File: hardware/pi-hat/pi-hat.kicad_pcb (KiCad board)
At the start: 2 copper layers, 65 x 56 mm, 88 parts, among them J1 PWR IN, J10 6-8, J11 PWM0, J12 PWM1, J13 KLPX-0848A-2-B, J14 KLPX-0848A-2-R, J2 A-F, J3 40HAT, J4 G-M, J5 N-Q, J6 PANEL_PWR, J7 PANEL_CTL, J8 2-5, J9 WP, Q1 DMG2305UX, Q2 DMMT5401, Q3 DMN6075S, Q4 ?, Q5 DMN6075S, U1 CAT24C32, U10 L78L33_SOT89, U11 L78L33_SOT89, U12 PCM5122PW, U2 CM1293A, U3 CM1293A, U4 CM1293A, U5 CM1293A, U6 CM1293A, U7 CM1293A, U8 MCP23S17_SO, U9 MCP23S17_SO

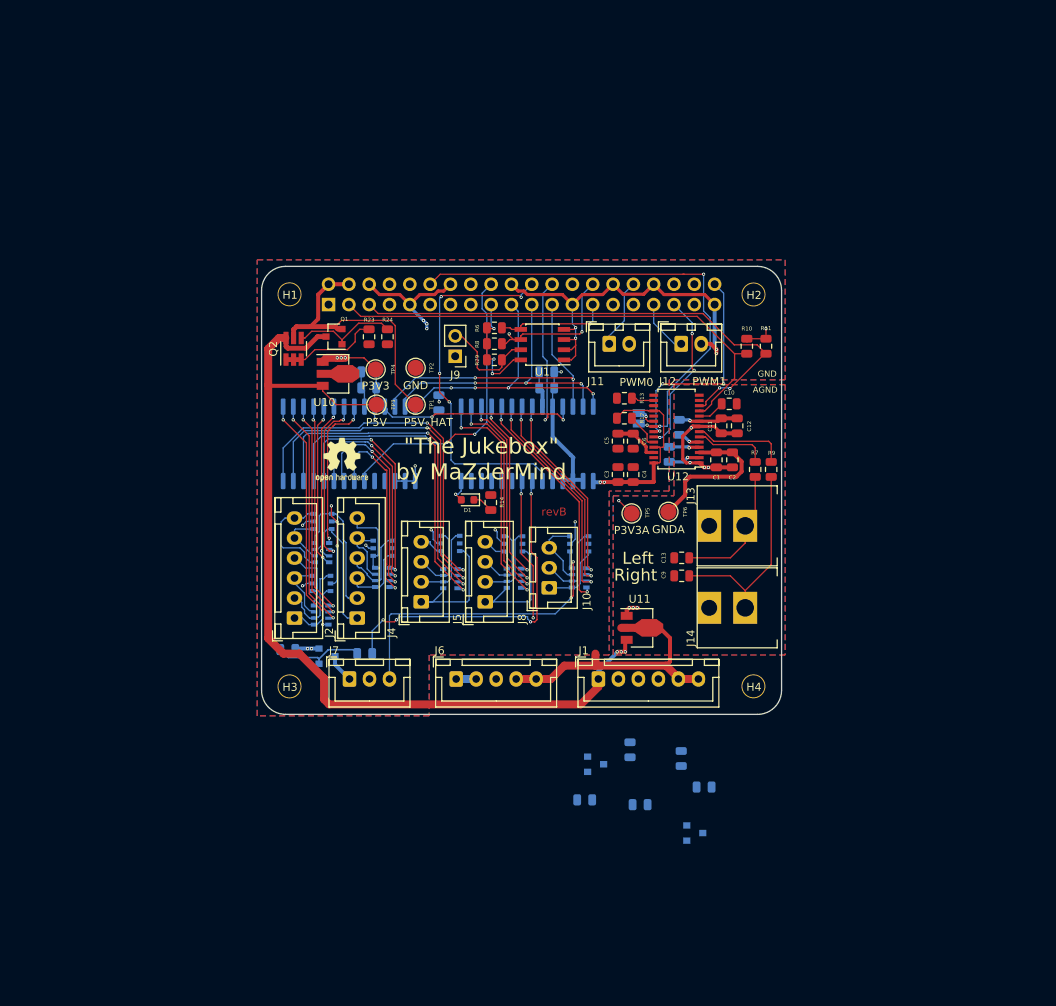
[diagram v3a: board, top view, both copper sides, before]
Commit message: re-configure board. route 30V and GND
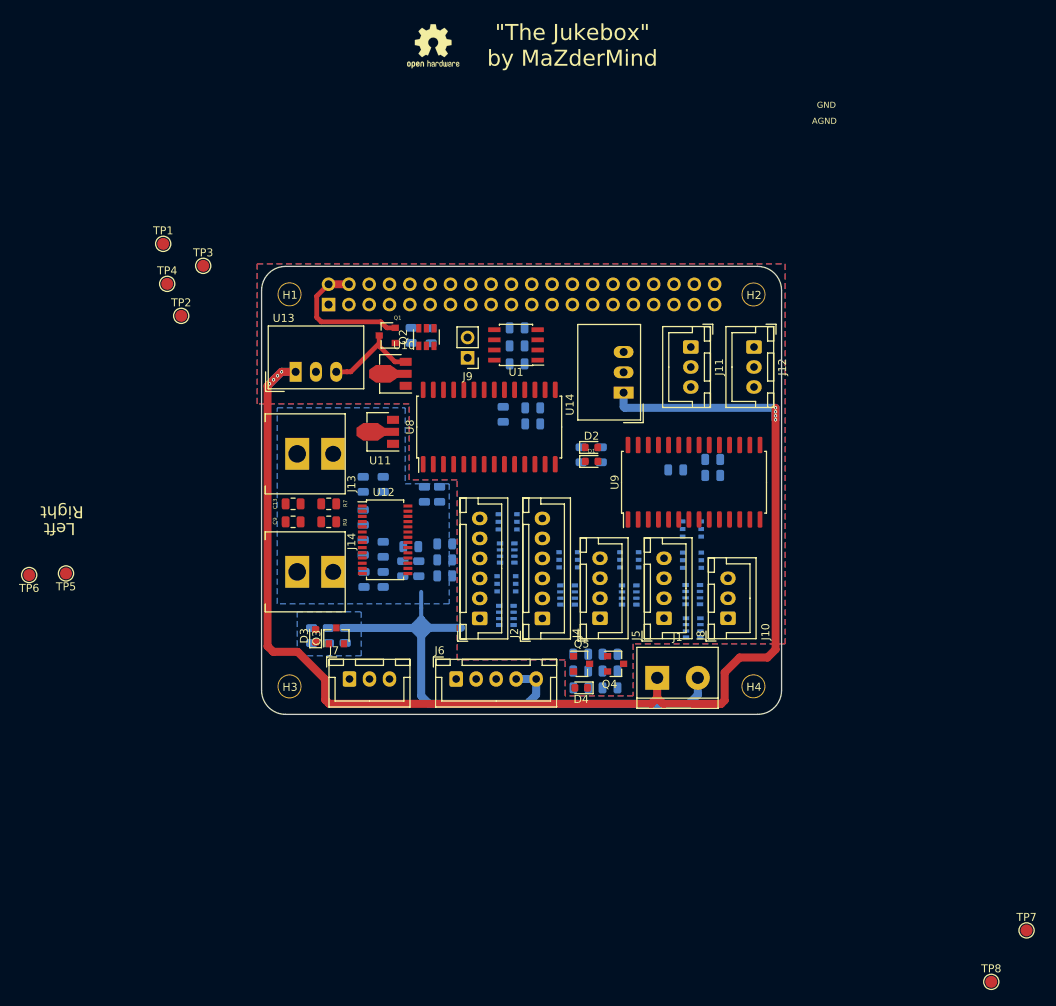
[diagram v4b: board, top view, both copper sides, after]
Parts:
- removed JP2: Jumper_NO_Small, Jumper:SolderJumper-2_P1.3mm_Open_Pad1.0x1.5mm
- added D3: SOLENOID, LED_SMD:LED_0603_1608Metric, F.Cu at (85.3, 107.0)
- added D4: PANEL, LED_SMD:LED_0603_1608Metric, F.Cu at (118.5, 113.5)
- added D5: MMSZ5239B-7-F (9.1V), Diode_SMD:D_0805_2012Metric, B.Cu at (122.1, 109.3)
- added R17: 10k, Resistor_SMD:R_0805_2012Metric, B.Cu at (130.3, 86.2)
- added R18: 100R, Resistor_SMD:R_0805_2012Metric, B.Cu at (84.8, 107.0)
- added R19: 100R, Resistor_SMD:R_0805_2012Metric, B.Cu at (122.1, 113.5)
- added R20: 100R, Resistor_SMD:R_0805_2012Metric, B.Cu at (121.0, 84.4)
- added TP7: P30V, TestPoint:TestPoint_Pad_D1.5mm, F.Cu at (174.2, 143.8)
- added TP8: P5V_LED, TestPoint:TestPoint_Pad_D1.5mm, F.Cu at (169.8, 150.2)
- added U13: TSR_2-2450, Converter_DCDC:Converter_DCDC_TRACO_TSR-1_THT, F.Cu at (82.8, 74.0)
- added U14: TSR_2-2450, Converter_DCDC:Converter_DCDC_TRACO_TSR-1_THT, F.Cu at (123.8, 76.6)
- C1, C10, C11, C12, C2, C3, C4, C5, C6, JP1, R10, R11, R12, R13, R14, R23, R24, R29, R6, R8: moved to B.Cu
- D1: value LED GN -> READY
- D2: value ? -> PLAY; footprint Diode_SMD:D_0805_2012Metric -> LED_SMD:LED_0603_1608Metric; moved to F.Cu
- J1: value PWR IN -> PWR_IN; footprint Connector_JST:JST_XH_B6B-XH-A_1x06_P2.50mm_Vertical -> TerminalBlock:TerminalBlock_bornier-2_P5.08mm
- J11: value PWM0 -> LED0; footprint Connector_JST:JST_XH_B2B-XH-A_1x02_P2.50mm_Vertical -> Connector_JST:JST_XH_B3B-XH-A_1x03_P2.50mm_Vertical
- J12: value PWM1 -> LED1; footprint Connector_JST:JST_XH_B2B-XH-A_1x02_P2.50mm_Vertical -> Connector_JST:JST_XH_B3B-XH-A_1x03_P2.50mm_Vertical
- Q2: footprint Package_TO_SOT_SMD:SOT-23-6_Handsoldering -> Package_TO_SOT_SMD:SOT-23-6
- Q3, Q5, U8, U9: moved to F.Cu
- Q4: value ? -> DMP4065S; moved to F.Cu
- R16: value 10k -> 5.6k
- R4: value 10k -> NC
- TP1, TP2, TP3, TP4, TP5, TP6: footprint TestPoint:TestPoint_Pad_D2.0mm -> TestPoint:TestPoint_Pad_D1.5mm
- moved TP6 80.3 mm to (49.5, 99.4), turned to 180 degrees
- moved TP5 71.1 mm to (54.1, 99.2), turned to 180 degrees
- moved J13 64.6 mm to (79.0, 84.2), turned to 0 degrees
- moved J14 64.2 mm to (79.0, 99.0), turned to 0 degrees
- moved R11 58.1 mm to (91.3, 100.0)
- moved R9 55.7 mm to (86.9, 92.8), turned to 0 degrees
- moved R10 54.0 mm to (93.8, 100.0)
- moved R7 53.5 mm to (86.9, 90.5), turned to 0 degrees
- moved OSHW1 52.9 mm to (100.0, 33.3)
- moved C13 49.0 mm to (82.5, 90.5)
- moved C9 49.0 mm to (82.5, 92.8)
- moved C2 46.3 mm to (91.2, 88.1)
- moved C12 45.5 mm to (96.2, 98.6)
- moved D2 45.1 mm to (119.8, 83.5)
- moved C10 43.6 mm to (97.2, 95.8), turned to 180 degrees
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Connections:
- net /IO_INT_A renamed /INT_U8
- net /IO_INT_B renamed /INT_U9
- net /LED renamed /READY_LED
- net /PANEL_30V renamed /PANEL_30V_OUT
- net /PANEL_SW renamed /PANEL_CTRL
- net /SOLENOID renamed /PANEL_SOLENOID_OUT
- net /SOLENOID_SW renamed /SOLENOID_CTRL
- D2 pad 1: /P30V -> Net-(D2-Pad1)
- D2 pad 2: Net-(D2-Pad2) -> /PLAY_LED
- J1 pad 1: /P5V -> /P30V
- J1 pad 2: (no net) -> GND
- J11 pad 1: /PWM0 -> /P5V_LED
- J11 pad 2: GND -> /PWM0
- J12 pad 1: /PWM1 -> /P5V_LED
- J12 pad 2: GND -> /PWM1
- J3 pad 19: /SPI_MISO -> /SPI_MOSI
- J3 pad 21: /SPI_MOSI -> /SPI_MISO
- J3 pad 24: /SPI_CS -> /SPI_CS_U8
- J3 pad 26: (no net) -> /SPI_CS_U9
- Q4 pad 1: Net-(D2-Pad2) -> Net-(D5-Pad2)
- R16 pad 2: Net-(D2-Pad2) -> Net-(D5-Pad2)
- R4 pad 1: Net-(D2-Pad2) -> Net-(D5-Pad2)
- R5 pad 2: /SPI_CS -> /SPI_CS_U8
- RN2 pad 7: /F -> /E
- RN2 pad 8: /E -> /F
- U12 pad 20: /DAC_SYSCLK -> (no net)
- U8 pad 11: /SPI_CS -> /SPI_CS_U8
- U8 pad 18: GND -> /P3V3
- U9 pad 11: /SPI_CS -> /SPI_CS_U9
- U9 pad 15: /P3V3 -> GND
- U9 pad 18: GND -> /P3V3
- U9 pad 27: (no net) -> /PLAY_LED
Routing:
- net /P30V: track 0.00 -> 169.5 mm, vias 0 -> 8
- net /P5V: track 116.6 -> 12.3 mm, vias 3 -> 0
- net GND: track 141.1 -> 71.2 mm, vias 19 -> 0
- net /I2C_SCL: track 63.5 -> 0.00 mm, vias 2 -> 0
- net /I2C_SDA: track 61.8 -> 0.00 mm
- net /PCM_CLK: track 60.2 -> 0.00 mm, vias 3 -> 0
- net /P3V3: track 59.1 -> 0.00 mm, vias 9 -> 0
- net /INT_U9: track 46.5 -> 0.00 mm, vias 4 -> 0
- net /SPI_CS: track 45.0 -> 0.00 mm, vias 3 -> 0
- net /Q: track 44.7 -> 0.00 mm, vias 2 -> 0
- net /P: track 43.9 -> 0.00 mm, vias 2 -> 0
- net /O: track 42.7 -> 0.00 mm, vias 2 -> 0
- net /SOLENOID_CTRL: track 42.6 -> 0.00 mm, vias 4 -> 0
- net /N: track 41.0 -> 0.00 mm, vias 2 -> 0
- net /ANY_KEY_IN: track 39.2 -> 0.00 mm, vias 2 -> 0
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- added copper zone on F.Cu, net /P3V3
- added copper zone on B.Cu, net GND
- added copper zone on B.Cu, net GNDA
- removed copper zone on B.Cu, net /P3V3
- removed copper zone on B.Cu, net /P3V3A
- removed copper zone on F.Cu, net GND
- removed copper zone on F.Cu, net GNDA
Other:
- net class 30V added: clearance 0.381, trace_width 0.15, via_dia 0.4, via_drill 0.2
- net class Default: clearance 0.2 -> 0.1778
- rule trace_clearance: 0.2 -> 0.1778
- board text removed: "30V"
- board text removed: "revB"

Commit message: route soundcard and 1st gpio extender
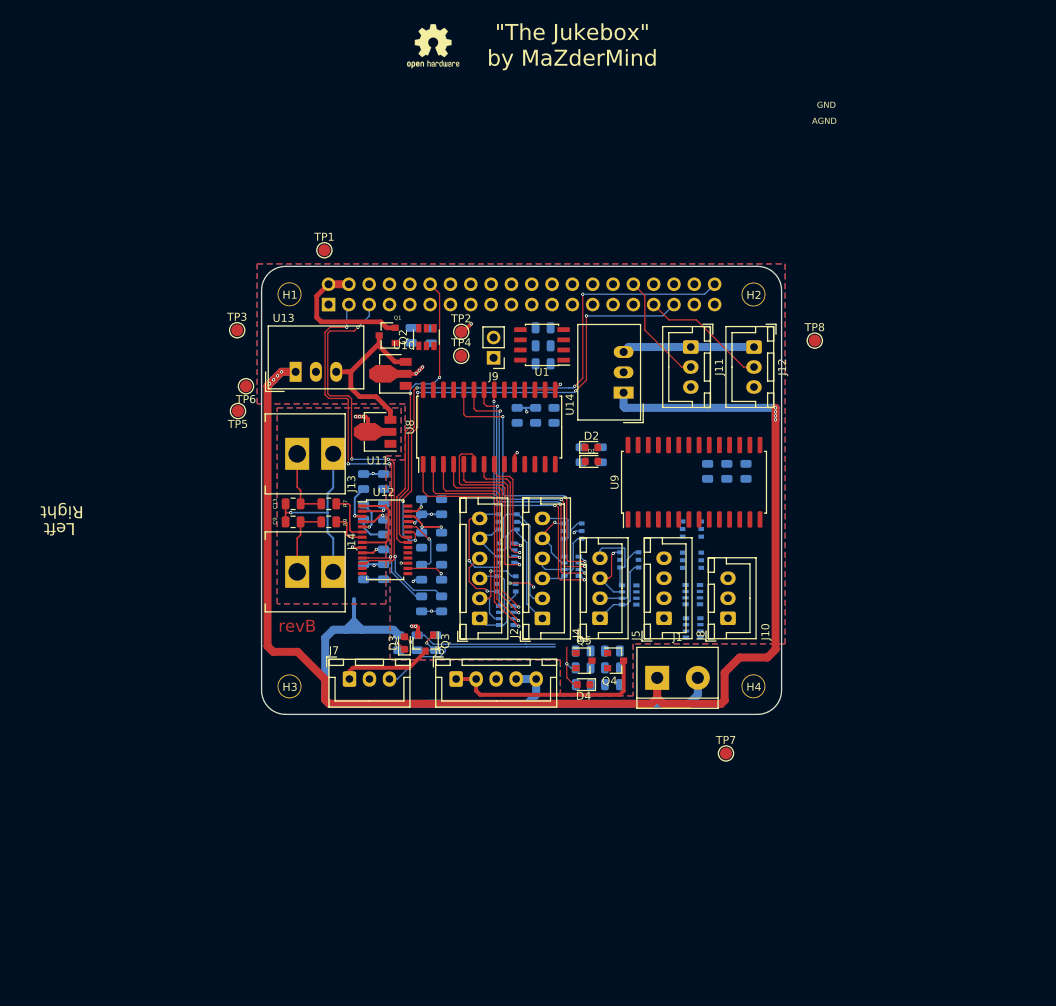
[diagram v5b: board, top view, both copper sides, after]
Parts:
- moved TP8 83.1 mm to (147.7, 70.1)
- moved TP7 43.6 mm to (136.6, 121.7)
- moved TP4 37.8 mm to (103.5, 72.0)
- moved TP6 35.9 mm to (76.6, 75.8)
- moved TP2 35.1 mm to (103.5, 69.0)
- moved TP5 29.6 mm to (75.6, 78.9)
- moved TP1 20.2 mm to (86.4, 58.8)
- moved R2 11.3 mm to (100.3, 107.8)
- moved Q3 11.2 mm to (99.0, 107.9), turned to 270 degrees
- moved D3 11.1 mm to (96.4, 107.9)
- moved R1 11.1 mm to (98.0, 107.9)
- moved R18 10.9 mm to (95.7, 107.9)
- moved R11 10.2 mm to (101.0, 103.0), turned to 90 degrees
- moved TP3 9.10 mm to (75.5, 68.8)
- moved JP1 8.40 mm to (90.1, 103.8)
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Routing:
- net /PCM_DATA: track 0.00 -> 69.2 mm, vias 0 -> 3
- net /PCM_FS: track 0.00 -> 63.5 mm, vias 0 -> 5
- net /I2C_SCL: track 0.00 -> 56.8 mm, vias 0 -> 4
- net /I2C_SDA: track 0.00 -> 52.7 mm, vias 0 -> 4
- net GNDA: track 2.00 -> 44.6 mm, vias 0 -> 6
- net /PCM_CLK: track 0.00 -> 37.5 mm, vias 0 -> 2
- net /M: track 0.00 -> 37.0 mm, vias 0 -> 3
- net /L: track 0.00 -> 36.4 mm, vias 0 -> 3
- net /K: track 0.00 -> 36.0 mm, vias 0 -> 3
- net /J: track 0.00 -> 35.5 mm, vias 0 -> 3
- net /A: track 0.00 -> 30.6 mm, vias 0 -> 1
- net /B: track 0.00 -> 28.9 mm, vias 0 -> 1
- net /C: track 0.00 -> 26.8 mm, vias 0 -> 1
- net /PANEL_30V_OUT: track 0.00 -> 26.6 mm
- net GND: track 71.2 -> 97.2 mm, vias 0 -> 10
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- added copper zone on F.Cu, net /P3V3A
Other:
- board text added: "revB"

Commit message: fix drc errors
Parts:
- moved D3 1.43 mm to (95.8, 106.6)
- moved R18 1.26 mm to (95.7, 106.6)
- moved R1 1.25 mm to (98.0, 106.6)
- moved R2 1.25 mm to (100.3, 106.6)
- moved Q3 1.20 mm to (99.1, 106.7)
- moved J5 0.25 mm to (121.1, 104.8)
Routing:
- net /ANY_KEY_IN: track 22.7 -> 11.0 mm
- net /SOLENOID_CTRL: track 20.0 -> 9.39 mm
- net /P30V: track 169.5 -> 165.3 mm, vias 8 -> 4
- net Net-(D3-Pad1): track 2.35 -> 0.00 mm, vias 1 -> 0
- net /PANEL_SOLENOID_OUT: track 11.6 -> 12.8 mm
- net GND: track 97.2 -> 96.9 mm, vias 10 -> 8

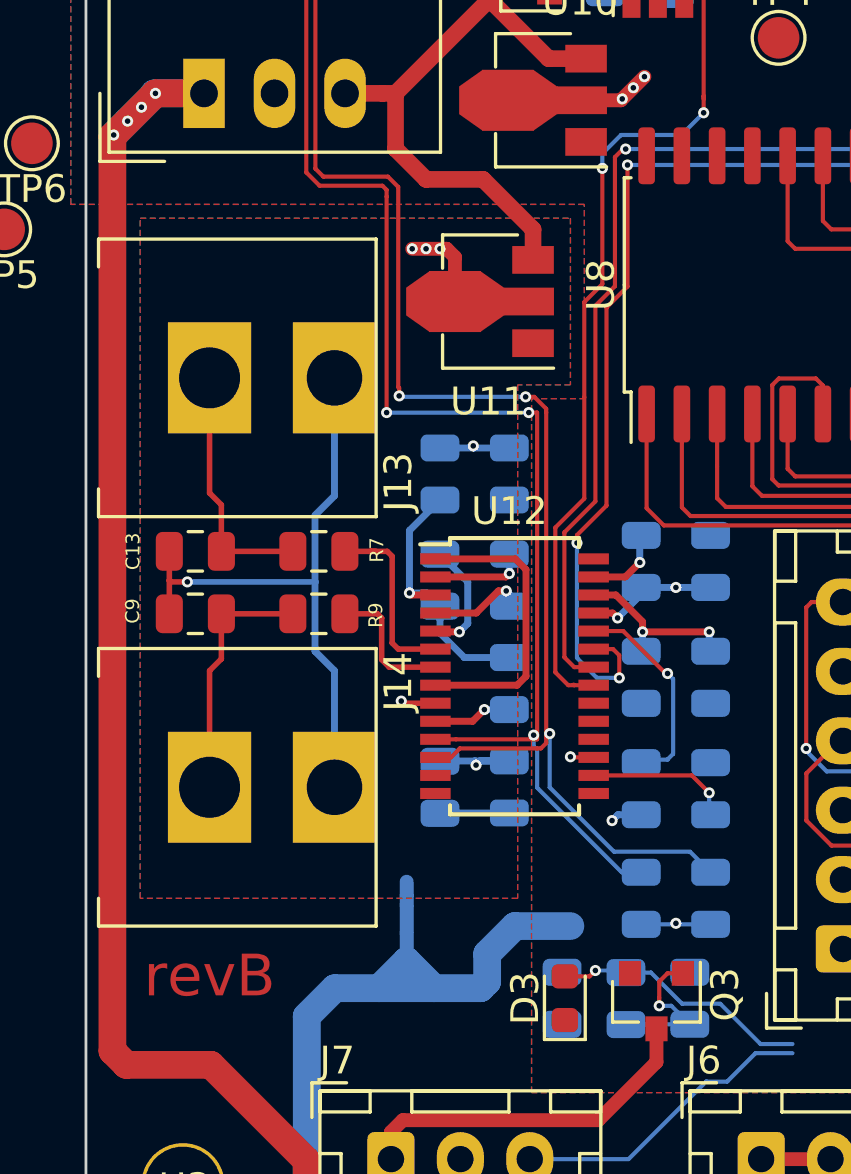
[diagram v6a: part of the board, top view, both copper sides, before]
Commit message: fix rca connector pinout
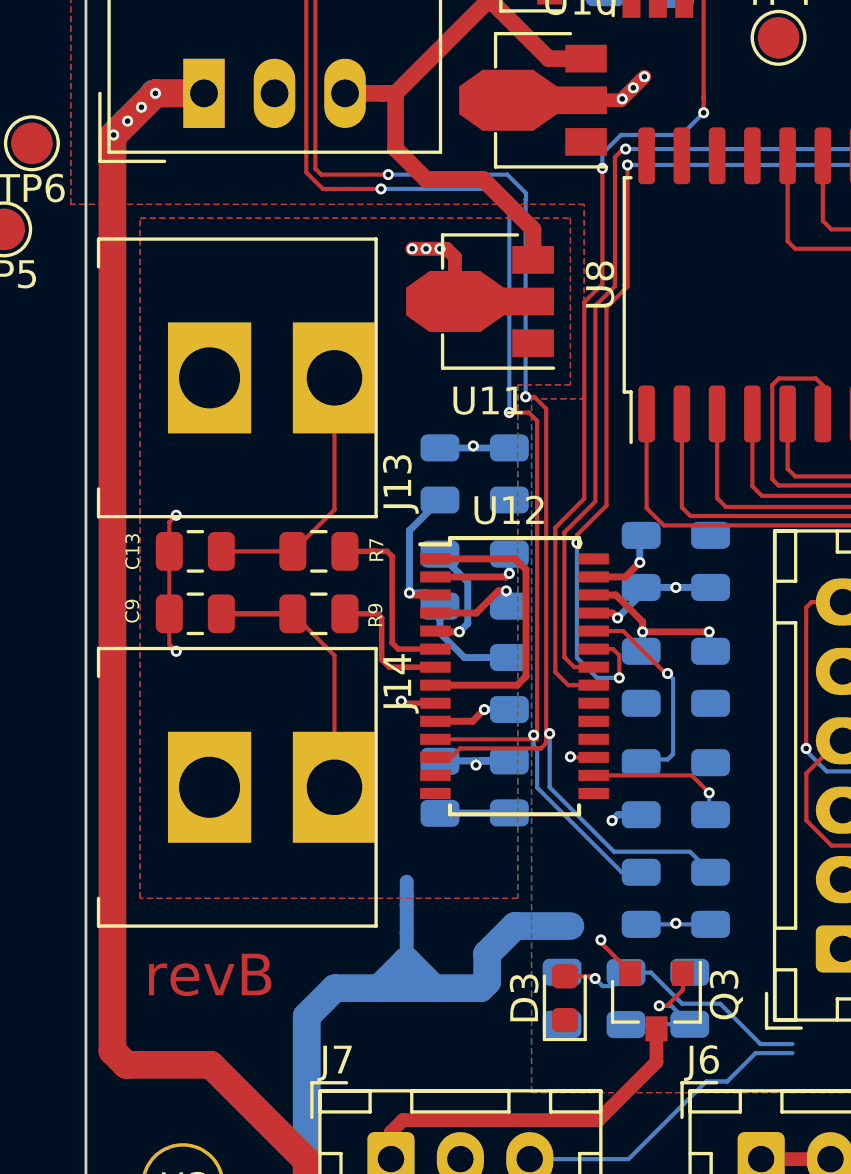
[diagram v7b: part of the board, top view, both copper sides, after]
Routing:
- net GNDA: track 44.6 -> 26.9 mm, vias 6 -> 7
- net GND: track 96.9 -> 98.5 mm, vias 8 -> 9

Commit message: fix routing
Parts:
- moved OSHW1 73.7 mm to (92.2, 106.6)
- moved JP1 42.6 mm to (131.0, 115.5), turned to 180 degrees
- moved TP3 26.3 mm to (101.5, 73.0)
- moved TP8 22.5 mm to (127.6, 80.3)
- moved TP5 20.2 mm to (93.4, 88.4)
- moved TP1 18.1 mm to (101.5, 68.8)
- moved TP6 17.2 mm to (90.8, 85.5)
- moved TP7 15.5 mm to (123.2, 114.0)
- moved U7 5.60 mm to (137.1, 96.6)
- moved R29 4.04 mm to (111.5, 69.6), turned to 270 degrees
- moved R6 2.53 mm to (116.0, 69.6), turned to 270 degrees
- moved D1 1.76 mm to (118.3, 84.3), turned to 90 degrees
- moved D2 1.65 mm to (121.2, 84.3), turned to 90 degrees
- moved TP4 1.35 mm to (104.5, 72.9)
- moved R8 1.11 mm to (113.8, 69.6), turned to 270 degrees
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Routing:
- net /SPI_CLK: track 0.00 -> 58.3 mm
- net GNDA: track 26.9 -> 83.7 mm, vias 7 -> 8
- net /SPI_MISO: track 0.00 -> 56.3 mm, vias 0 -> 2
- net /SPI_MOSI: track 0.00 -> 55.2 mm, vias 0 -> 2
- net /SPI_CS_U9: track 0.00 -> 53.9 mm, vias 0 -> 3
- net /SOLENOID_CTRL: track 9.61 -> 62.3 mm, vias 1 -> 4
- net /O: track 0.00 -> 51.5 mm, vias 0 -> 3
- net /P3V3: track 17.2 -> 68.6 mm, vias 9 -> 31
- net /Q: track 0.00 -> 51.0 mm, vias 0 -> 3
- net /P: track 0.00 -> 50.1 mm, vias 0 -> 3
- net GND: track 98.5 -> 48.9 mm, vias 9 -> 13
- net /N: track 0.00 -> 49.3 mm, vias 0 -> 3
- net /SPI_CS_U8: track 0.00 -> 46.5 mm, vias 0 -> 2
- net /INT_U9: track 0.00 -> 42.7 mm, vias 0 -> 1
- net /ANY_KEY_IN: track 11.0 -> 53.1 mm, vias 0 -> 2
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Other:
- board text removed: ""The Jukebox" by MaZderMind"
